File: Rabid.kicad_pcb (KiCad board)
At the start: 2 copper layers, 343.4 x 121.9 mm, 193 parts, among them J1 USB Connector, J3 GPIO Debug Header, SW1 Esc, SW10 A, SW102 →, SW103 BootSel Switch, SW104 Reset Switch, SW11 Z, SW12 LMeta, SW13 F1, SW14 2, SW15 W, SW16 S, SW17 X, SW18 LAlt, SW19 F2, SW2 Tilde, SW20 3, SW21 E, SW22 D, SW23 C, SW25 F3, SW26 4, SW27 R, SW28 F, SW29 V, SW3 Tab, SW31 F4, SW32 5, SW33 T, SW34 G, SW35 B, SW37 F5, SW38 6, SW39 Y, SW4 CapsLk, SW40 H, SW41 N, SW42 Space, SW43 F6, SW44 7, SW45 U, SW46 J, SW47 M, SW49 F7, SW5 LShift, SW50 8, SW51 I, SW52 K, SW53 ,, SW55 F8, SW56 9, SW57 O, SW58 L, SW59 ., SW6 LCtrl, SW61 F9, SW62 0, SW63 P, SW64 ;, SW65 /, SW66 AltGr, SW67 F10, SW68 -, SW69 [, SW70 ", SW71 RShift, SW72 RMeta, SW73 F11, SW74 =, SW75 ], SW76 ↲, SW78 Fn, SW79 F12, SW8 1, SW80 BkSpc, SW81 \, SW84 RCtrl, SW85 PrtSc, SW86 Ins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

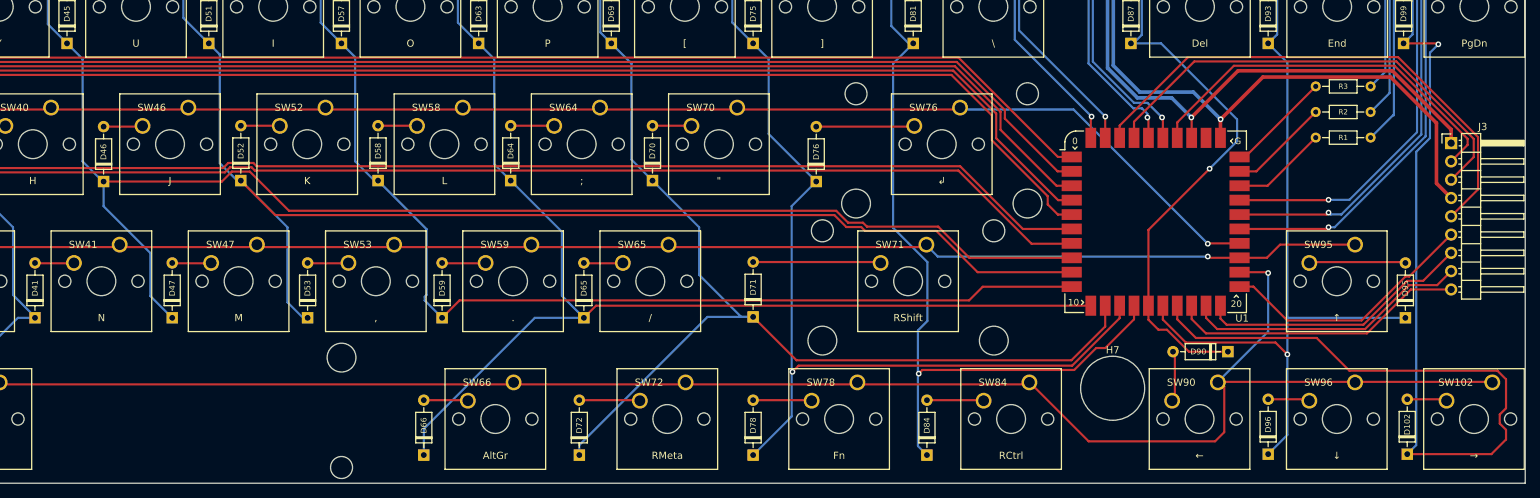
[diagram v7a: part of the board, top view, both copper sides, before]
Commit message: Add project title/author/revision/url to silkscreen.
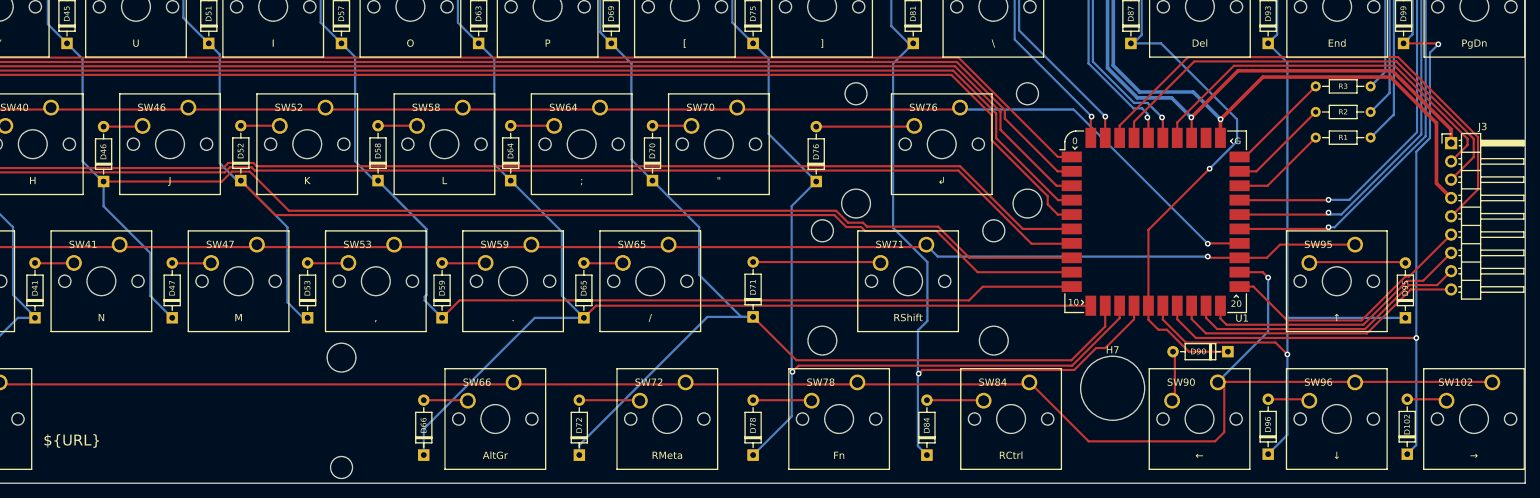
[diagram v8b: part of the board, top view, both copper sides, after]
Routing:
- net ColQ: track 187.5 -> 149.0 mm, vias 1 -> 2
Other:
- board text added: "${TITLE} ${REVISION} ${COMPANY} ${URL}"
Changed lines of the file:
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@@
     )
   )
+  (property "COMPANY" "Sean D. Cline")
+  (property "REVISION" "V1.0")
+  (property "TITLE" "RabidKeyboard")
+  (property "URL" "https://sdcline.com/RabidKeyboard")
   (net 0 "")
   (net 1 "ColA")
@@
     (effects (font (size 1.5 1.5) (thickness 0.3)) (justify right mirror))
   )
+  (gr_text "${TITLE} ${REVISION}\n${COMPANY}\n${URL}" (at 177.673 190.5) (layer "F.SilkS")
+    (effects (font (size 1.5 1.5) (thickness 0.3)) (justify left))
+  )
   (dimension (type aligned) (layer "Cmts.User")
     (pts (xy 323.85 76.073) (xy 328.676 76.073))
@@
   (segment (start 367.411 111.125) (end 372.4656 111.125) (width 0.3) (layer "F.Cu") (net 101))
   (segment (start 367.411 130.175) (end 372.5418 130.175) (width 0.3) (layer "F.Cu") (net 102))
-  (segment (start 380.746 188.444242) (end 379.873479 189.316763) (width 0.3) (layer "F.Cu") (net 103))
-  (segment (start 379.873479 190.565637) (end 380.746 191.438158) (width 0.3) (layer "F.Cu") (net 103))
-  (segment (start 380.746 192.786) (end 378.714 194.818) (width 0.3) (layer "F.Cu") (net 103))
-  (segment (start 359.003489 183.235489) (end 379.554969 183.235489) (width 0.3) (layer "F.Cu") (net 103))
-  (segment (start 379.554969 183.235489) (end 380.746 184.42652) (width 0.3) (layer "F.Cu") (net 103))
-  (segment (start 354.457 178.689) (end 359.003489 183.235489) (width 0.3) (layer "F.Cu") (net 103))
-  (segment (start 380.746 184.42652) (end 380.746 188.444242) (width 0.3) (layer "F.Cu") (net 103))
-  (segment (start 380.746 191.438158) (end 380.746 192.786) (width 0.3) (layer "F.Cu") (net 103))
-  (segment (start 335.105 175.212) (end 335.105 176.101) (width 0.3) (layer "F.Cu") (net 103))
-  (segment (start 335.105 176.101) (end 337.693 178.689) (width 0.3) (layer "F.Cu") (net 103))
+  (segment (start 335.105 176.101) (end 335.105 175.212) (width 0.3) (layer "F.Cu") (net 103))
+  (segment (start 337.693 178.689) (end 335.105 176.101) (width 0.3) (layer "F.Cu") (net 103))
+  (segment (start 368.3 178.689) (end 337.693 178.689) (width 0.3) (layer "F.Cu") (net 103))
   (segment (start 371.221 137.795) (end 366.522 137.795) (width 0.3) (layer "F.Cu") (net 103))
-  (segment (start 379.873479 189.316763) (end 379.873479 190.565637) (width 0.3) (layer "F.Cu") (net 103))
-  (segment (start 337.693 178.689) (end 354.457 178.689) (width 0.3) (layer "F.Cu") (net 103))
   (segment (start 371.348 137.922) (end 371.221 137.795) (width 0.3) (layer "F.Cu") (net 103))
-  (segment (start 378.714 194.818) (end 367.03 194.818) (width 0.3) (layer "F.Cu") (net 103))
+  (via (at 368.3 178.689) (size 0.8) (drill 0.4) (layers "F.Cu" "B.Cu") (net 103))
   (via (at 371.348 137.922) (size 0.8) (drill 0.4) (layers "F.Cu" "B.Cu") (net 103))
+  (segment (start 370.19008 139.07992) (end 371.348 137.922) (width 0.3) (layer "B.Cu") (net 103))
   (segment (start 369.390511 93.419511) (end 369.390511 100.380987) (width 0.3) (layer "B.Cu") (net 103))
+  (segment (start 368.279511 152.846188) (end 370.19008 150.935618) (width 0.3) (layer "B.Cu") (net 103))
+  (segment (start 368.279511 178.668511) (end 368.279511 152.846188) (width 0.3) (layer "B.Cu") (net 103))
   (segment (start 366.522 118.745) (end 367.771511 119.994511) (width 0.3) (layer "B.Cu") (net 103))
   (segment (start 367.792 117.475) (end 366.522 118.745) (width 0.3) (layer "B.Cu") (net 103))
   (segment (start 367.771511 136.545489) (end 366.522 137.795) (width 0.3) (layer "B.Cu") (net 103))
   (segment (start 367.792 101.979498) (end 367.792 117.475) (width 0.3) (layer "B.Cu") (net 103))
+  (segment (start 370.19008 150.935618) (end 370.19008 139.07992) (width 0.3) (layer "B.Cu") (net 103))
+  (segment (start 368.3 178.689) (end 368.279511 178.709489) (width 0.3) (layer "B.Cu") (net 103))
   (segment (start 368.279511 193.568489) (end 367.03 194.818) (width 0.3) (layer "B.Cu") (net 103))
-  (segment (start 368.279511 152.846188) (end 368.279511 193.568489) (width 0.3) (layer "B.Cu") (net 103))
-  (segment (start 371.348 137.922) (end 370.19008 139.07992) (width 0.3) (layer "B.Cu") (net 103))
+  (segment (start 368.279511 178.709489) (end 368.279511 193.568489) (width 0.3) (layer "B.Cu") (net 103))
   (segment (start 369.390511 100.380987) (end 367.792 101.979498) (width 0.3) (layer "B.Cu") (net 103))
-  (segment (start 370.19008 150.935618) (end 368.279511 152.846188) (width 0.3) (layer "B.Cu") (net 103))
   (segment (start 366.776 90.678) (end 369.390511 93.292511) (width 0.3) (layer "B.Cu") (net 103))
   (segment (start 367.771511 119.994511) (end 367.771511 136.545489) (width 0.3) (layer "B.Cu") (net 103))
-  (segment (start 370.19008 139.07992) (end 370.19008 150.935618) (width 0.3) (layer "B.Cu") (net 103))
+  (segment (start 368.3 178.689) (end 368.279511 178.668511) (width 0.3) (layer "B.Cu") (net 103))
   (segment (start 288.036 105.664) (end 289.166721 104.533279) (width 0.3) (layer "F.Cu") (net 104))
   (segment (start 289.166721 104.533279) (end 319.417279 104.533279) (width 0.3) (layer "F.Cu") (net 104))
@@
   (segment (start 340.36 193.04) (end 341.63 191.77) (width 0.3) (layer "F.Cu") (net 107))
   (segment (start 314.579 184.8104) (end 322.8086 193.04) (width 0.3) (layer "F.Cu") (net 107))
-  (segment (start 347.614 169.56) (end 347.726 169.672) (width 0.3) (layer "F.Cu") (net 107))
   (segment (start 340.741 184.785) (end 378.841 184.785) (width 0.3) (layer "F.Cu") (net 107))
   (segment (start 341.63 185.42) (end 340.995 184.785) (width 0.3) (layer "F.Cu") (net 107))
-  (segment (start 343.501 169.56) (end 347.614 169.56) (width 0.3) (layer "F.Cu") (net 107))
+  (segment (start 347.726 170.307) (end 346.979 169.56) (width 0.3) (layer "F.Cu") (net 107))
+  (segment (start 346.979 169.56) (end 343.501 169.56) (width 0.3) (layer "F.Cu") (net 107))
   (segment (start 322.8086 193.04) (end 340.36 193.04) (width 0.3) (layer "F.Cu") (net 107))
-  (via (at 347.726 169.672) (size 0.8) (drill 0.4) (layers "F.Cu" "B.Cu") (net 107))
-  (segment (start 347.726 169.672) (end 347.726 177.8) (width 0.3) (layer "B.Cu") (net 107))
+  (via (at 347.726 170.307) (size 0.8) (drill 0.4) (layers "F.Cu" "B.Cu") (net 107))
+  (segment (start 347.726 170.307) (end 347.726 177.8) (width 0.3) (layer "B.Cu") (net 107))
   (segment (start 347.726 177.8) (end 340.741 184.785) (width 0.3) (layer "B.Cu") (net 107))
   (segment (start 356.108 159.512) (end 356.06 159.56) (width 0.3) (layer "F.Cu") (net 108))
